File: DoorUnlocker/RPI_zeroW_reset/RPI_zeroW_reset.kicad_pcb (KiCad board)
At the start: 2 copper layers, 7.6 x 10.7 mm, 4 parts, among them J1 Conn_01x02, SW1 Button, U1 TPL5111

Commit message: pcb updates
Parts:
- added C1: C_Small, Capacitors:0805, F.Cu at (113.6, 66.5)
- added J2: Conn_01x01, Connector_PinHeader_2.54mm:PinHeader_1x01_P2.54mm_Vertical, F.Cu at (99.1, 63.4)
- added Q1: BSS83P, Silicon-Standard:SOT323, F.Cu at (141.4, 66.9)
- added R2: R, Resistor_SMD:R_0805_2012Metric, F.Cu at (116.9, 66.5)
- added RV1: R_POT, CustomFP:Bourns_TC33X-2, F.Cu at (131.2, 66.6)
- added SW2: SW_SPST, CustomFP:SWITCH_SPDT_PTH, F.Cu at (106.3, 67.7)
- J1: value Conn_01x02 -> RPI_Conn; footprint CustomFP:PinHeader_1x02_P2.54mm_Horizontal -> Connector_PinHeader_2.54mm:PinHeader_2x02_P2.54mm_Vertical; moved to B.Cu
- R1: footprint Resistors:1206 -> Resistor_SMD:R_0805_2012Metric; moved to F.Cu
- SW1: value Button -> SW_Push
- U1: footprint kicad-open-modules:SOT-23-6 -> Package_TO_SOT_SMD:SOT-23-6
- moved J1 36.8 mm to (144.8, 63.5), turned to 270 degrees
- moved R1 29.3 mm to (138.3, 66.6), turned to 90 degrees
- moved U1 27.7 mm to (134.8, 66.6)
- moved SW1 20.6 mm to (125.7, 65.0), turned to 180 degrees
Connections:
- J1 pad 1: Net-(J1-Pad1) -> /GPIO26
- J1 pad 2: Net-(J1-Pad2) -> GND
- R1 pad 1: Net-(J1-Pad2) -> Net-(Q1-Pad1)
- R1 pad 2: Net-(R1-Pad2) -> +5V
- SW1 pad 1: Net-(R1-Pad2) -> Net-(RV1-Pad1)
- SW1 pad 2: Net-(J1-Pad1) -> +5V
- U1 pad 1: Net-(J1-Pad1) -> +5V
- U1 pad 2: Net-(J1-Pad2) -> GND
- U1 pad 3: Net-(R1-Pad2) -> Net-(RV1-Pad1)
- U1 pad 4: (no net) -> /GPIO26
- U1 pad 5: Net-(J1-Pad1) -> Net-(Q1-Pad1)
- U1 pad 6: Net-(J1-Pad1) -> +5V
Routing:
- net +5V: track 0.00 -> 35.4 mm
- net GND: track 0.00 -> 35.0 mm, vias 0 -> 4
- net /GPIO26: track 0.00 -> 33.5 mm, vias 0 -> 2
- net Net-(J1-Pad1): track 12.0 -> 0.00 mm
- net Net-(RV1-Pad1): track 0.00 -> 8.53 mm
- net Net-(J1-Pad2): track 6.83 -> 0.00 mm, vias 1 -> 0
- net /RUN: track 0.00 -> 6.50 mm
- net Net-(J2-Pad1): track 0.00 -> 6.49 mm
- net Net-(R1-Pad2): track 6.27 -> 0.00 mm, vias 1 -> 0
- net Net-(Q1-Pad1): track 0.00 -> 5.31 mm
- added copper zone on B.Cu, net GND
- added copper zone on F.Cu, net GND
- removed copper zone on B.Cu, net Net-(J1-Pad2)
- removed copper zone on F.Cu, net Net-(J1-Pad2)
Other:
- board size 7.6 x 10.7 mm -> 50.9 x 7.1 mm
- net class Default: clearance 0.2 -> 0.15; trace_width 0.25 -> 0.12
- rule trace_clearance: 0.2 -> 0.15
- rule trace_min: 0.2 -> 0.1
- board text added: "Scott's Creative Designs RPIWZ Reset - V1"

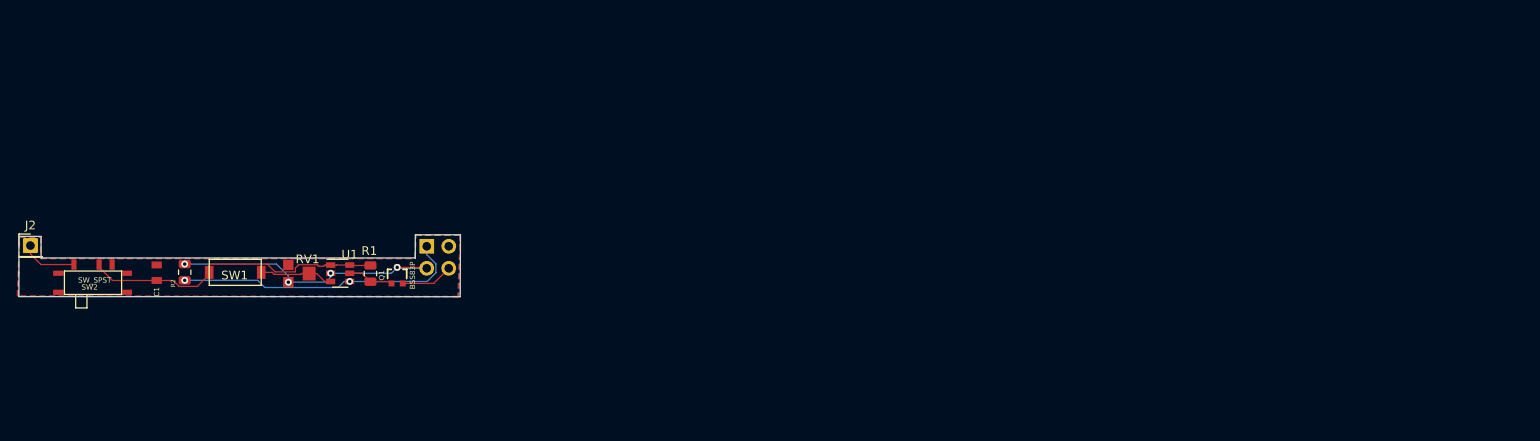
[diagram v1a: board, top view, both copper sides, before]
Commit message: Updated Door Unlocker and PS
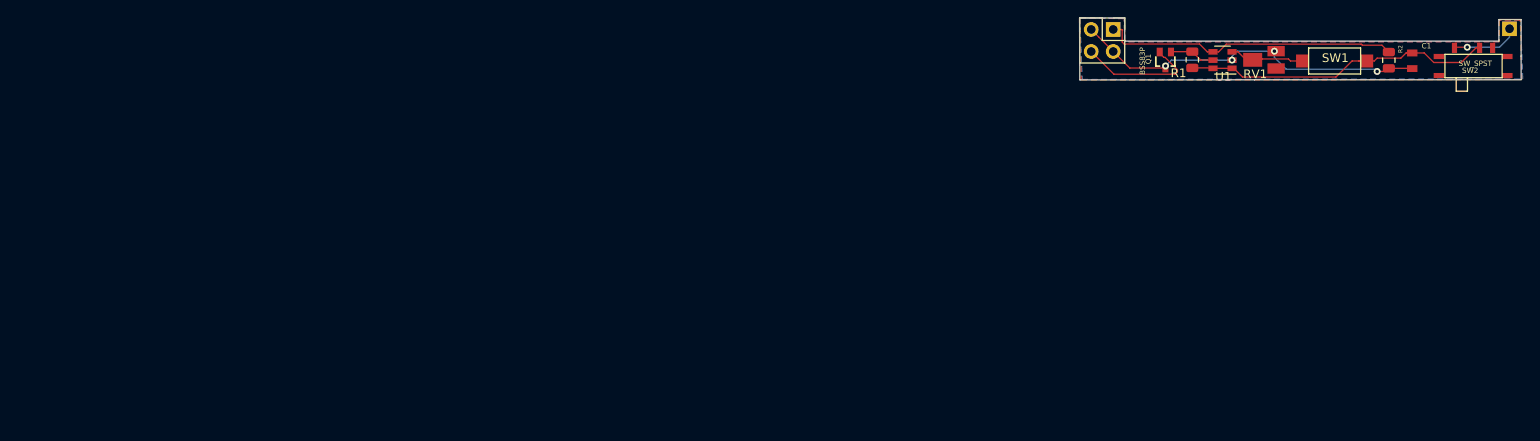
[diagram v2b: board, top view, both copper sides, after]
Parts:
- J1: moved to F.Cu
- J2: moved to B.Cu
- Q1: footprint Silicon-Standard:SOT323 -> CustomFP:SOT323
- moved J2 172.4 mm to (269.7, 38.4), turned to 180 degrees
- moved SW2 161.2 mm to (265.5, 42.7)
- moved C1 146.9 mm to (258.4, 42.1), turned to 90 degrees
- moved R2 141.0 mm to (255.7, 42.0), turned to 90 degrees
- moved SW1 122.7 mm to (246.5, 43.6), turned to 0 degrees
- moved RV1 111.7 mm to (240.1, 42.0), turned to 90 degrees
- moved U1 104.7 mm to (236.6, 42.0), turned to 180 degrees
- moved R1 97.9 mm to (233.1, 42.0), turned to 270 degrees
- moved Q1 92.0 mm to (230.0, 42.0), turned to 180 degrees
- moved J1 83.0 mm to (224.0, 38.5)
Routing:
- net /RUN: track 6.50 -> 14.4 mm
- net GND: track 35.0 -> 41.5 mm
- net Net-(J2-Pad1): track 6.49 -> 7.83 mm, vias 0 -> 1
- net /GPIO26: track 33.5 -> 34.4 mm, vias 2 -> 0
- net +5V: track 35.4 -> 36.0 mm
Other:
- outline, holes or cut-outs redrawn
